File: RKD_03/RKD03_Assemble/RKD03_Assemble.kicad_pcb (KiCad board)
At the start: 2 copper layers, 97.7 x 97.6 mm, 29 parts, among them J1 GROVE-CONNECTOR-DIP_4P-2.0_, SW1 RotaryEncoder_Switch, SW10 SW_Push, SW2 SW_Push, SW3 RotaryEncoder_Switch, SW4 SW_Push, SW5 RotaryEncoder_Switch, SW6 SW_Push, SW7 RotaryEncoder_Switch, SW8 SW_Push, SW9 RotaryEncoder_Switch, U1 Pico

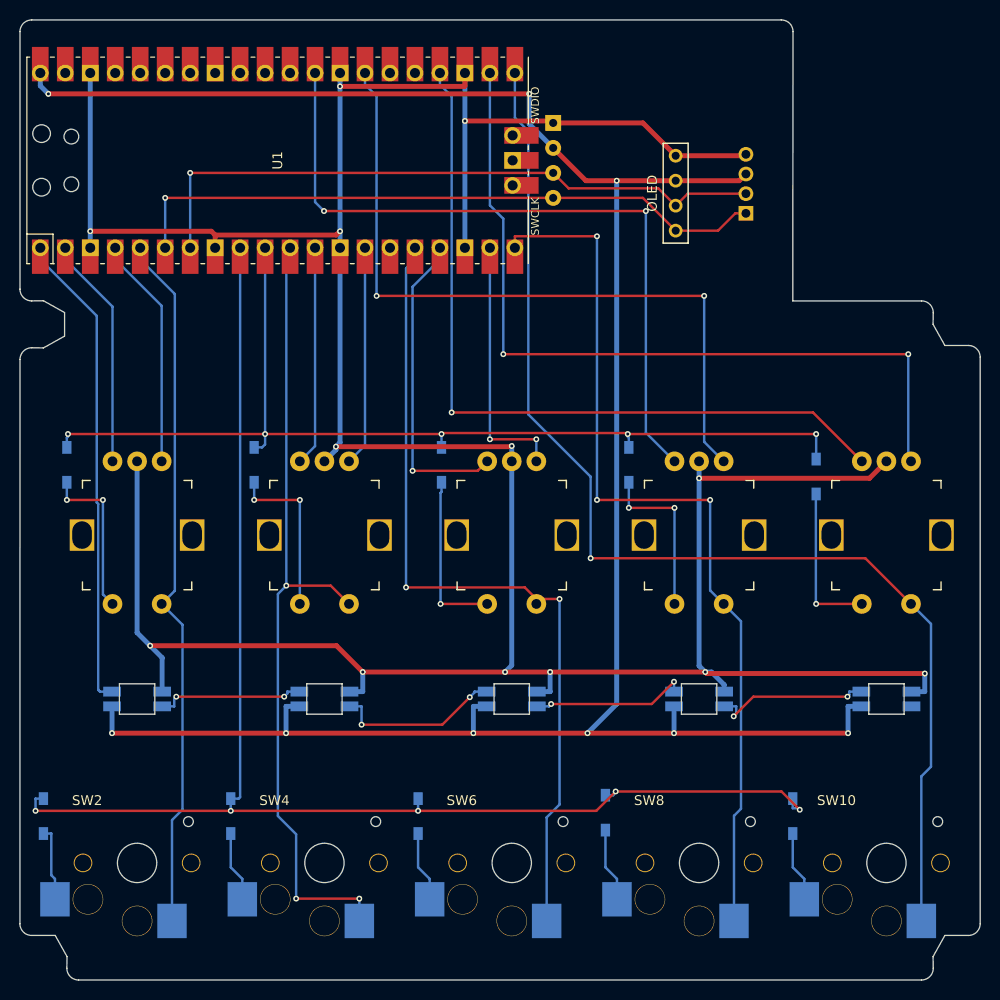
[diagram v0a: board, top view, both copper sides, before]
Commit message: LEDの誤り修正1.01
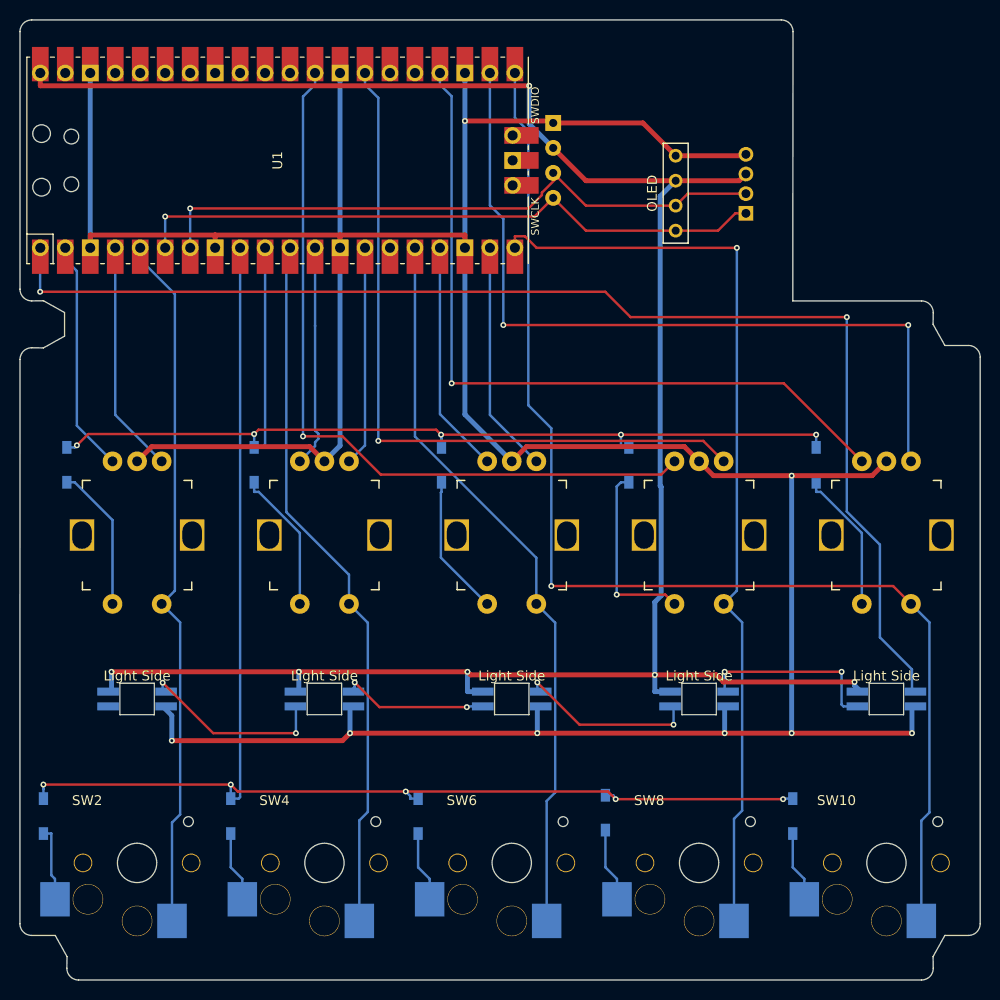
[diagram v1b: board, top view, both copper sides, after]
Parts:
- LED1, LED2, LED3, LED4, LED5: footprint BrownSugar_KBD:RGBLED_SK6812MINI-E -> kbd_Parts:LED_SK6812MINI-E_BL; moved to F.Cu
- moved LED1 76.2 mm to (131.0, 85.7)
- moved LED5 76.2 mm to (54.8, 85.7)
- moved LED2 38.1 mm to (111.9, 85.7)
- moved LED4 38.1 mm to (73.8, 85.7)
- moved D9 1.19 mm to (123.8, 61.9)
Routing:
- net LED: track 48.9 -> 128.4 mm, vias 0 -> 2
- net Col1: track 83.3 -> 72.4 mm, vias 3 -> 0
- net Col2: track 84.8 -> 74.7 mm, vias 2 -> 0
- net VCC: track 229.1 -> 219.6 mm, vias 9 -> 6
- net RE3_B: track 31.8 -> 23.7 mm, vias 1 -> 0
- net Row1: track 143.7 -> 139.6 mm
- net Net-(LED1-DOUT): track 15.1 -> 19.3 mm
- net Col4: track 120.5 -> 124.4 mm
- net RE4_B: track 73.8 -> 77.4 mm, vias 2 -> 1
- net GND: track 346.9 -> 350.2 mm, vias 13 -> 8
- net Net-(LED4-DOUT): track 16.6 -> 19.4 mm
- net Net-(D5-A): track 17.1 -> 14.3 mm, vias 1 -> 0
- net RE3_A: track 26.4 -> 23.7 mm, vias 2 -> 0
- net Net-(D3-A): track 17.0 -> 14.6 mm, vias 2 -> 0
- net Col3: track 92.3 -> 94.4 mm, vias 3 -> 1
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
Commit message: RKD03V2作成中
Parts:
- added D1: D, kbd_Parts:Diode_SMD, F.Cu at (45.2, 59.5)
- added D10: D, kbd_Parts:Diode_SMD, F.Cu at (102.4, 59.5)
- added D13: D, kbd_Parts:Diode_SMD, F.Cu at (121.4, 59.5)
- added D4: D, kbd_Parts:Diode_SMD, F.Cu at (64.3, 59.5)
- added D7: D, kbd_Parts:Diode_SMD, F.Cu at (83.3, 59.5)
- added SW1: SW_Push, kbd_SW:Choc_Hotswap_1u, F.Cu at (54.8, 64.3)
- added SW10: SW_Push, kbd_SW:Choc_Hotswap_1u, F.Cu at (111.9, 64.3)
- added SW13: SW_Push, kbd_SW:Choc_Hotswap_1u, F.Cu at (131.0, 64.3)
- added SW4: SW_Push, kbd_SW:Choc_Hotswap_1u, F.Cu at (73.8, 64.3)
- added SW7: SW_Push, kbd_SW:Choc_Hotswap_1u, F.Cu at (92.9, 64.3)
- moved LED1 33.3 mm to (131.0, 52.4)
- moved LED2 33.3 mm to (111.9, 52.4)
- moved LED3 33.3 mm to (92.9, 52.4)
- moved LED4 33.3 mm to (73.8, 52.4)
- moved LED5 33.3 mm to (54.8, 52.4)
- moved D11 14.3 mm to (104.8, 76.2)
- moved D14 14.3 mm to (123.8, 76.2)
- moved D2 14.3 mm to (47.6, 76.2)
- moved D5 14.3 mm to (66.7, 76.2)
- moved D8 14.3 mm to (85.7, 76.2)
- moved SW11 14.3 mm to (111.9, 83.3)
- moved SW14 14.3 mm to (131.0, 83.3)
- moved SW2 14.3 mm to (54.8, 83.3)
- moved SW5 14.3 mm to (73.8, 83.3)
- moved SW8 14.3 mm to (92.9, 83.3)
- renumbered D7 to D11, D8 to D12, D9 to D14, D10 to D15, D1 to D2, D2 to D3, D3 to D5, D4 to D6, D5 to D8, D6 to D9, SW7 to SW11, SW8 to SW12, SW9 to SW14, SW10 to SW15, SW1 to SW2, SW2 to SW3, SW3 to SW5, SW4 to SW6, SW5 to SW8, SW6 to SW9
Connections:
- D11 pad 1: Row0 -> Row1
- D12 pad 1: Row1 -> Row2
- D14 pad 1: Row0 -> Row1
- D15 pad 1: Row1 -> Row2
- D2 pad 1: Row0 -> Row1
- D3 pad 1: Row1 -> Row2
- D5 pad 1: Row0 -> Row1
- D6 pad 1: Row1 -> Row2
- D8 pad 1: Row0 -> Row1
- D9 pad 1: Row1 -> Row2
- J1 pad 3: VCC -> 3v3
- OL1 pad 3: VCC -> 3v3
- OL2 pad 3: VCC -> 3v3
- U1 pad 15: unconnected-(U1-GPIO11-Pad15) -> Row2
- U1 pad 36: unconnected-(U1-3V3-Pad36)_1 -> 3v3
- U1 pad 39: unconnected-(U1-VSYS-Pad39)_1 -> VCC
- U1 pad 40: VCC -> unconnected-(U1-VBUS-Pad40)_1
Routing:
- net GND: track 350.2 -> 0.00 mm, vias 8 -> 0
- net VCC: track 219.6 -> 0.00 mm, vias 6 -> 0
- net Row1: track 139.6 -> 0.00 mm, vias 5 -> 0
- net LED: track 128.4 -> 0.00 mm, vias 2 -> 0
- net Col4: track 124.4 -> 0.00 mm, vias 1 -> 0
- net Row0: track 104.4 -> 0.00 mm, vias 5 -> 0
- net Col3: track 94.4 -> 0.00 mm, vias 1 -> 0
- net RE5_A: track 81.4 -> 0.00 mm, vias 2 -> 0
- net RE4_B: track 77.4 -> 0.00 mm, vias 1 -> 0
- net RE5_B: track 77.1 -> 0.00 mm, vias 1 -> 0
- net Col2: track 74.7 -> 0.00 mm
- net RE4_A: track 74.0 -> 0.00 mm, vias 1 -> 0
- net Col1: track 72.4 -> 0.00 mm
- net Col0: track 71.6 -> 0.00 mm
- net SDA: track 65.1 -> 0.00 mm, vias 1 -> 0
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
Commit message: RKD03 試行錯誤中
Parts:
- removed J1: GROVE-CONNECTOR-DIP_4P-2.0_, OPL_Connector:GROVE-HW4-2.0
- moved OL2 7.48 mm to (102.4, 35.9)

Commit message: RKD03_手直し
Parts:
- removed D15: D, kbd_Parts:Diode_SMD
- removed SW15: SW_Push, kbd_SW:Choc_Hotswap_1u
- SW1, SW10, SW13, SW3, SW4, SW6, SW7, SW9: footprint kbd_SW:Choc_Hotswap_1u -> Rikkodo_FootPrint:rkd_Choc_v2_Hotswap_1u
- SW12: footprint kbd_SW:Choc_Hotswap_1u -> Rikkodo_FootPrint:rkd_Choc_v2_Hotswap_2u
- U1: footprint RPi_Pico:RPi_Pico_SMD_TH -> Rikkodo_FootPrint:rkd_RPi_Pico_TH
- moved SW12 9.52 mm to (121.4, 102.4)
- turned LED1 to 0 degrees
- turned LED2 to 0 degrees
- turned LED4 to 0 degrees
- turned LED3 to 0 degrees
- turned LED5 to 0 degrees
- renumbered LED5 to LED1, LED4 to LED2, LED2 to LED4, LED1 to LED5
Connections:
- LED1 pad 1: unconnected-(LED5-DOUT-Pad1) -> Net-(LED1-DOUT)
- LED1 pad 3: Net-(LED4-DOUT) -> LED
- LED2 pad 1: Net-(LED4-DOUT) -> Net-(LED2-DOUT)
- LED2 pad 3: Net-(LED3-DOUT) -> Net-(LED1-DOUT)
- LED4 pad 1: Net-(LED2-DOUT) -> Net-(LED4-DOUT)
- LED4 pad 3: Net-(LED1-DOUT) -> Net-(LED3-DOUT)
- LED5 pad 1: Net-(LED1-DOUT) -> unconnected-(LED5-DOUT-Pad1)
- LED5 pad 3: LED -> Net-(LED4-DOUT)
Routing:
- net GND: track 0.00 -> 307.5 mm, vias 0 -> 8
- net VCC: track 0.00 -> 198.8 mm, vias 0 -> 7
- net Row1: track 0.00 -> 122.5 mm, vias 0 -> 6
- net Row2: track 0.00 -> 120.3 mm, vias 0 -> 4
- net Col4: track 0.00 -> 106.5 mm, vias 0 -> 2
- net Row0: track 0.00 -> 100.6 mm, vias 0 -> 5
- net RE5_B: track 0.00 -> 98.5 mm, vias 0 -> 1
- net Col3: track 0.00 -> 95.9 mm, vias 0 -> 1
- net RE5_A: track 0.00 -> 90.2 mm, vias 0 -> 2
- net RE4_A: track 0.00 -> 86.8 mm, vias 0 -> 1
- net RE4_B: track 0.00 -> 85.8 mm, vias 0 -> 1
- net Col2: track 0.00 -> 84.0 mm, vias 0 -> 2
- net Col1: track 0.00 -> 76.5 mm, vias 0 -> 1
- net Col0: track 0.00 -> 71.6 mm
- net 3v3: track 0.00 -> 52.2 mm, vias 0 -> 1
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
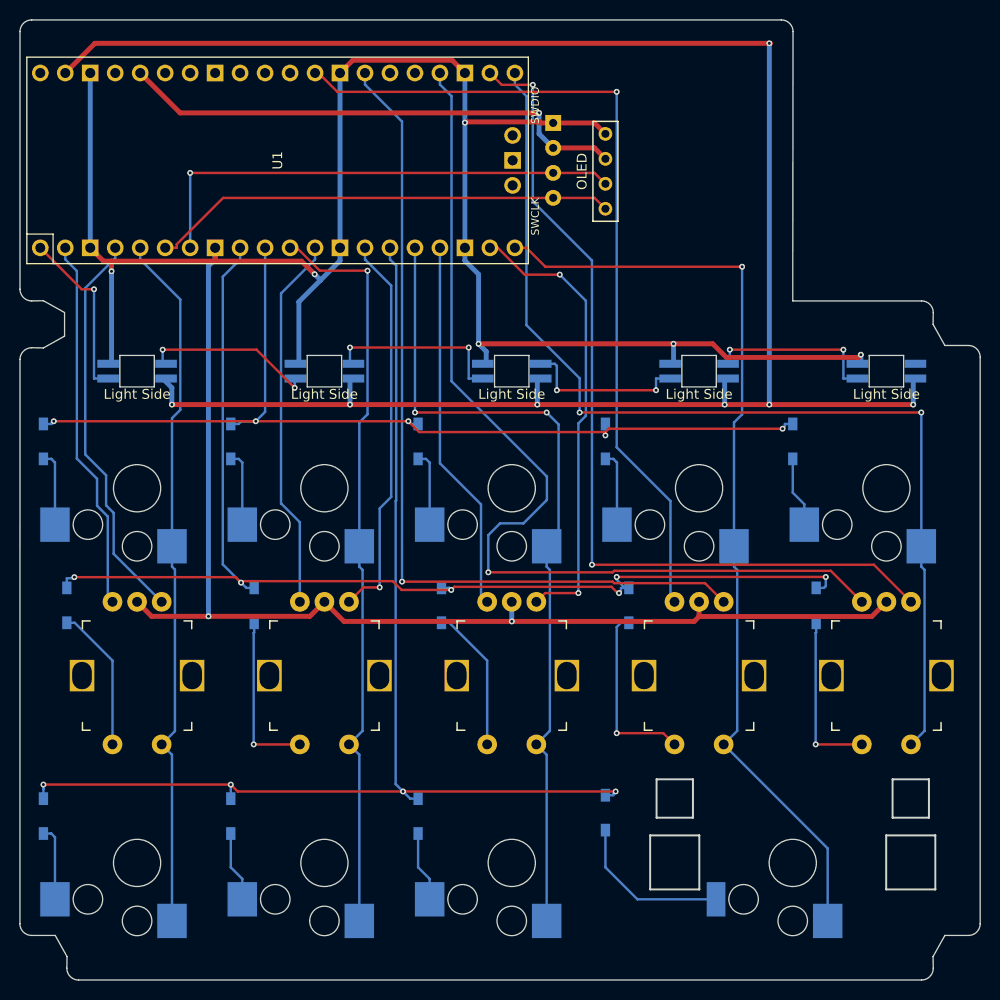
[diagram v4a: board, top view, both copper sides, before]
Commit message: RKD03 LED微調整
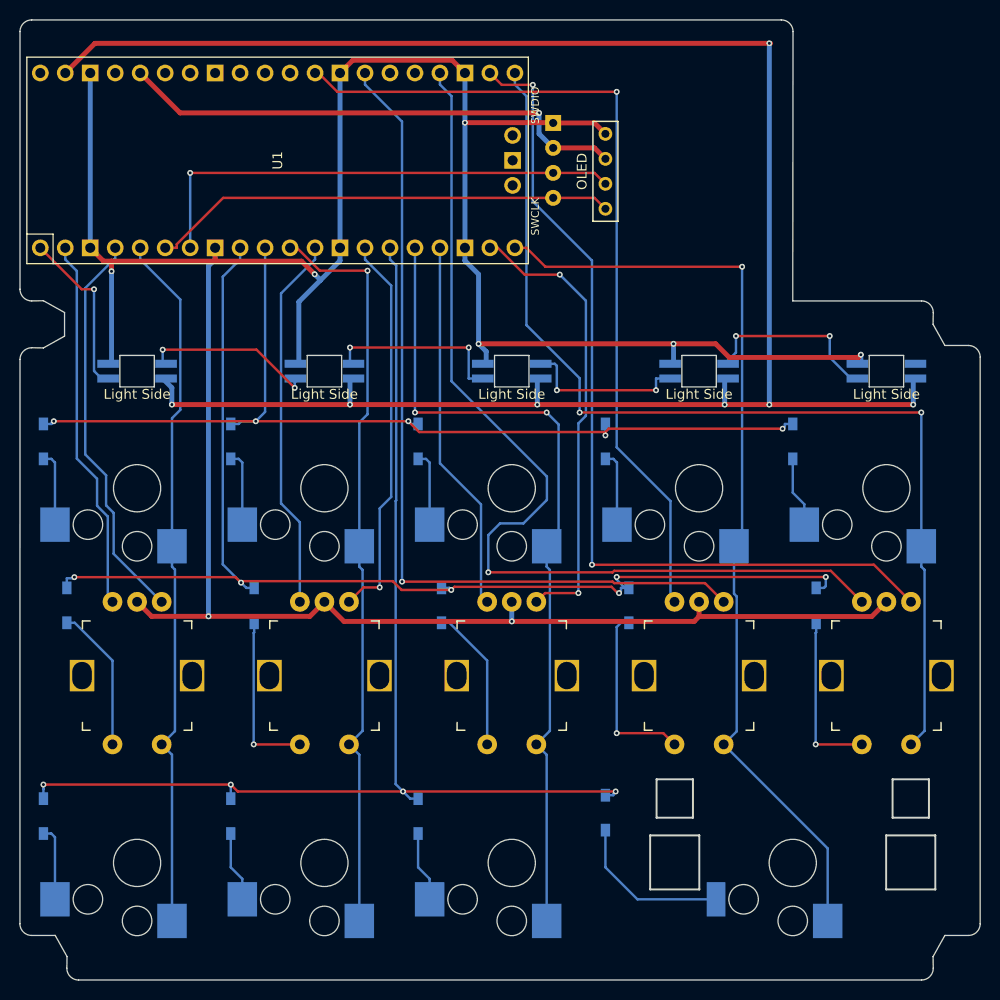
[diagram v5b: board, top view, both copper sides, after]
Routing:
- net Net-(LED4-DOUT): track 17.9 -> 19.1 mm
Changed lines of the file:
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@@
 	)
 	(segment
-		(start 88.1806 27.0421)
-		(end 88.1063 27.1164)
+		(start 52.1688 41.1989)
+		(end 52.1688 42.2359)
 		(width 0.5)
 		(layer "F.Cu")
@@
 	)
 	(segment
+		(start 113.604025 49.6068)
+		(end 114.991125 50.9939)
+		(width 0.5)
+		(layer "F.Cu")
+		(net 13)
+	)
+	(segment
 		(start 62.7063 39.8462)
 		(end 62.7063 41.1989)
@@
 	)
 	(segment
+		(start 97.0813 27.1462)
+		(end 97.0513 27.1162)
+		(width 0.5)
+		(layer "F.Cu")
+		(net 13)
+	)
+	(segment
+		(start 114.991125 50.9939)
+		(end 128.0902 50.9939)
+		(width 0.5)
+		(layer "F.Cu")
+		(net 13)
+	)
+	(segment
 		(start 51.359 41.1989)
 		(end 52.1688 41.1989)
@@
 	)
 	(segment
-		(start 113.3075 49.6068)
-		(end 114.6946 50.9939)
-		(width 0.5)
-		(layer "F.Cu")
-		(net 13)
-	)
-	(segment
 		(start 129.4759 77.3366)
 		(end 130.9688 75.8437)
@@
 	)
 	(segment
+		(start 102.3938 28.2575)
+		(end 101.2825 27.1462)
+		(width 0.5)
+		(layer "F.Cu")
+		(net 13)
+	)
+	(segment
 		(start 54.7688 75.8437)
 		(end 56.2445 77.3194)
@@
 	)
 	(segment
-		(start 102.3938 28.2575)
-		(end 101.2825 27.1462)
-		(width 0.5)
-		(layer "F.Cu")
-		(net 13)
-	)
-	(segment
 		(start 86.8063 20.7662)
 		(end 88.1063 22.0662)
@@
 	)
 	(segment
+		(start 88.1065 27.1162)
+		(end 88.1063 27.1164)
+		(width 0.5)
+		(layer "F.Cu")
+		(net 13)
+	)
+	(segment
 		(start 75.8093 77.8342)
 		(end 92.8688 77.8342)
@@
 	)
 	(segment
+		(start 109.3188 49.6068)
+		(end 113.604025 49.6068)
+		(width 0.5)
+		(layer "F.Cu")
+		(net 13)
+	)
+	(segment
+		(start 97.0513 27.1162)
+		(end 88.1065 27.1162)
+		(width 0.5)
+		(layer "F.Cu")
+		(net 13)
+	)
+	(segment
 		(start 101.2825 27.1462)
 		(end 97.0813 27.1462)
@@
 	)
 	(segment
-		(start 109.3188 49.6068)
-		(end 113.3075 49.6068)
-		(width 0.5)
-		(layer "F.Cu")
-		(net 13)
-	)
-	(segment
-		(start 97.0813 27.1462)
-		(end 95.8196 27.1462)
+		(start 128.0902 50.9939)
+		(end 128.3688 50.7153)
 		(width 0.5)
 		(layer "F.Cu")
@@
 		(net 13)
 	)
-	(segment
-		(start 128.0902 50.9939)
-		(end 128.3688 50.7153)
-		(width 0.5)
-		(layer "F.Cu")
-		(net 13)
-	)
-	(segment
-		(start 114.6946 50.9939)
-		(end 128.0902 50.9939)
-		(width 0.5)
-		(layer "F.Cu")
-		(net 13)
-	)
-	(segment
-		(start 52.1688 41.1989)
-		(end 52.1688 42.2359)
-		(width 0.5)
-		(layer "F.Cu")
-		(net 13)
-	)
-	(segment
-		(start 95.8196 27.1462)
-		(end 95.7155 27.0421)
-		(width 0.5)
-		(layer "F.Cu")
-		(net 13)
-	)
-	(segment
-		(start 95.7155 27.0421)
-		(end 88.1806 27.0421)
-		(width 0.5)
-		(layer "F.Cu")
-		(net 13)
-	)
 	(via
 		(at 89.4942 49.6068)
@@
 	)
 	(segment
+		(start 115.7438 89.0187)
+		(end 114.4188 90.3437)
+		(width 0.25)
+		(layer "B.Cu")
+		(net 19)
+	)
+	(segment
+		(start 116.2956 69.3669)
+		(end 116.2956 41.7673)
+		(width 0.25)
+		(layer "B.Cu")
+		(net 19)
+	)
+	(segment
+		(start 115.4688 75.019867)
+		(end 115.7438 75.294867)
+		(width 0.25)
+		(layer "B.Cu")
+		(net 19)
+	)
+	(segment
+		(start 115.7438 75.294867)
+		(end 115.7438 89.0187)
+		(width 0.25)
+		(layer "B.Cu")
+		(net 19)
+	)
+	(segment
 		(start 115.4688 70.1937)
-		(end 115.4688 57.6066)
-		(width 0.25)
-		(layer "B.Cu")
-		(net 19)
-	)
-	(segment
-		(start 115.7979 88.9646)
-		(end 114.4188 90.3437)
-		(width 0.25)
-		(layer "B.Cu")
-		(net 19)
-	)
-	(segment
-		(start 115.4688 57.6066)
-		(end 116.2956 56.7798)
+		(end 116.2956 69.3669)
 		(width 0.25)
 		(layer "B.Cu")
@@
 	)
 	(segment
-		(start 115.7979 72.5995)
-		(end 115.7979 88.9646)
-		(width 0.25)
-		(layer "B.Cu")
-		(net 19)
-	)
-	(segment
-		(start 115.4688 72.2704)
-		(end 115.7979 72.5995)
-		(width 0.25)
-		(layer "B.Cu")
-		(net 19)
-	)
-	(segment
-		(start 116.2956 56.7798)
-		(end 116.2956 41.7673)
-		(width 0.25)
-		(layer "B.Cu")
-		(net 19)
-	)
-	(segment
 		(start 115.4688 70.1937)
-		(end 115.4688 72.2704)
+		(end 115.4688 75.019867)
 		(width 0.25)
 		(layer "B.Cu")
@@
 	)
 	(segment
+		(start 50.3921 52.3707)
+		(end 51.1588 53.1374)
+		(width 0.25)
+		(layer "B.Cu")
+		(net 21)
+	)
+	(segment
+		(start 51.1588 53.1374)
+		(end 52.1688 53.1374)
+		(width 0.25)
+		(layer "B.Cu")
+		(net 21)
+	)
+	(segment
 		(start 50.3921 44.057812)
-		(end 50.3921 53.1374)
-		(width 0.25)
-		(layer "B.Cu")
-		(net 21)
-	)
-	(segment
-		(start 50.3921 53.1374)
-		(end 52.1688 53.1374)
+		(end 50.3921 52.3707)
 		(width 0.25)
 		(layer "B.Cu")
@@
 	)
 	(segment
-		(start 126.5921 50.2031)
-		(end 115.0443 50.2031)
+		(start 115.6706 48.815625)
+		(end 125.204625 48.815625)
 		(width 0.25)
 		(layer "F.Cu")
@@
 	)
 	(via
-		(at 115.0443 50.2031)
+		(at 115.6706 48.815625)
 		(size 0.6)
 		(drill 0.3)
@@
 	)
 	(via
-		(at 126.5921 50.2031)
+		(at 125.204625 48.815625)
 		(size 0.6)
 		(drill 0.3)
@@
 	)
 	(segment
-		(start 115.0443 51.112)
-		(end 115.0443 50.2031)
+		(start 115.6706 50.4857)
+		(end 114.5188 51.6375)
 		(width 0.25)
 		(layer "B.Cu")
@@
 	)
 	(segment
-		(start 114.5188 51.6375)
-		(end 115.0443 51.112)
+		(start 115.6706 48.815625)
+		(end 115.6706 50.4857)
 		(width 0.25)
 		(layer "B.Cu")
@@
 	)
 	(segment
-		(start 126.5921 53.1375)
-		(end 126.5921 50.2031)
+		(start 125.204625 50.983325)
+		(end 127.3588 53.1375)
 		(width 0.25)
 		(layer "B.Cu")
@@
 	)
 	(segment
-		(start 128.3688 53.1375)
-		(end 126.5921 53.1375)
-		(width 0.25)
-		(layer "B.Cu")
+		(start 125.204625 48.815625)
+		(end 125.204625 50.983325)
+		(width 0.25)
+		(layer "B.Cu")
+		(net 47)
+	)
+	(segment
+		(start 127.3588 53.1375)
+		(end 128.3688 53.1375)
+		(width 0.25)
+		(layer "B.Cu")

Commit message: RKD03 V1V2に修正
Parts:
- SW1, SW10, SW13, SW3, SW4, SW6, SW7, SW9: footprint Rikkodo_FootPrint:rkd_Choc_v2_Hotswap_1u -> Rikkodo_FootPrint:rkd_Choc_v1v2_Hotswap_1u
- SW12: footprint Rikkodo_FootPrint:rkd_Choc_v2_Hotswap_2u -> Rikkodo_FootPrint:rkd_Choc_v1v2_Hotswap_2u
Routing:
- net Col2: track 84.0 -> 86.0 mm
